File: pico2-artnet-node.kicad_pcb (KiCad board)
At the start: 2 copper layers, 84.6 x 157.4 mm, 59 parts, among them J2 NC3FAAH, J3 NC3FAAH, J4 NC3FAAH, J5 NC3FAAH, J6 USB_C_Receptacle_PowerOnly_6P, U1 W5500-EVB-PICO2, U2 CA-IS2092A, U3 CA-IS2092A, U4 CA-IS2092A, U5 CA-IS2092A, U6 WIZPoE Hat, U8 AMS1117-3.3

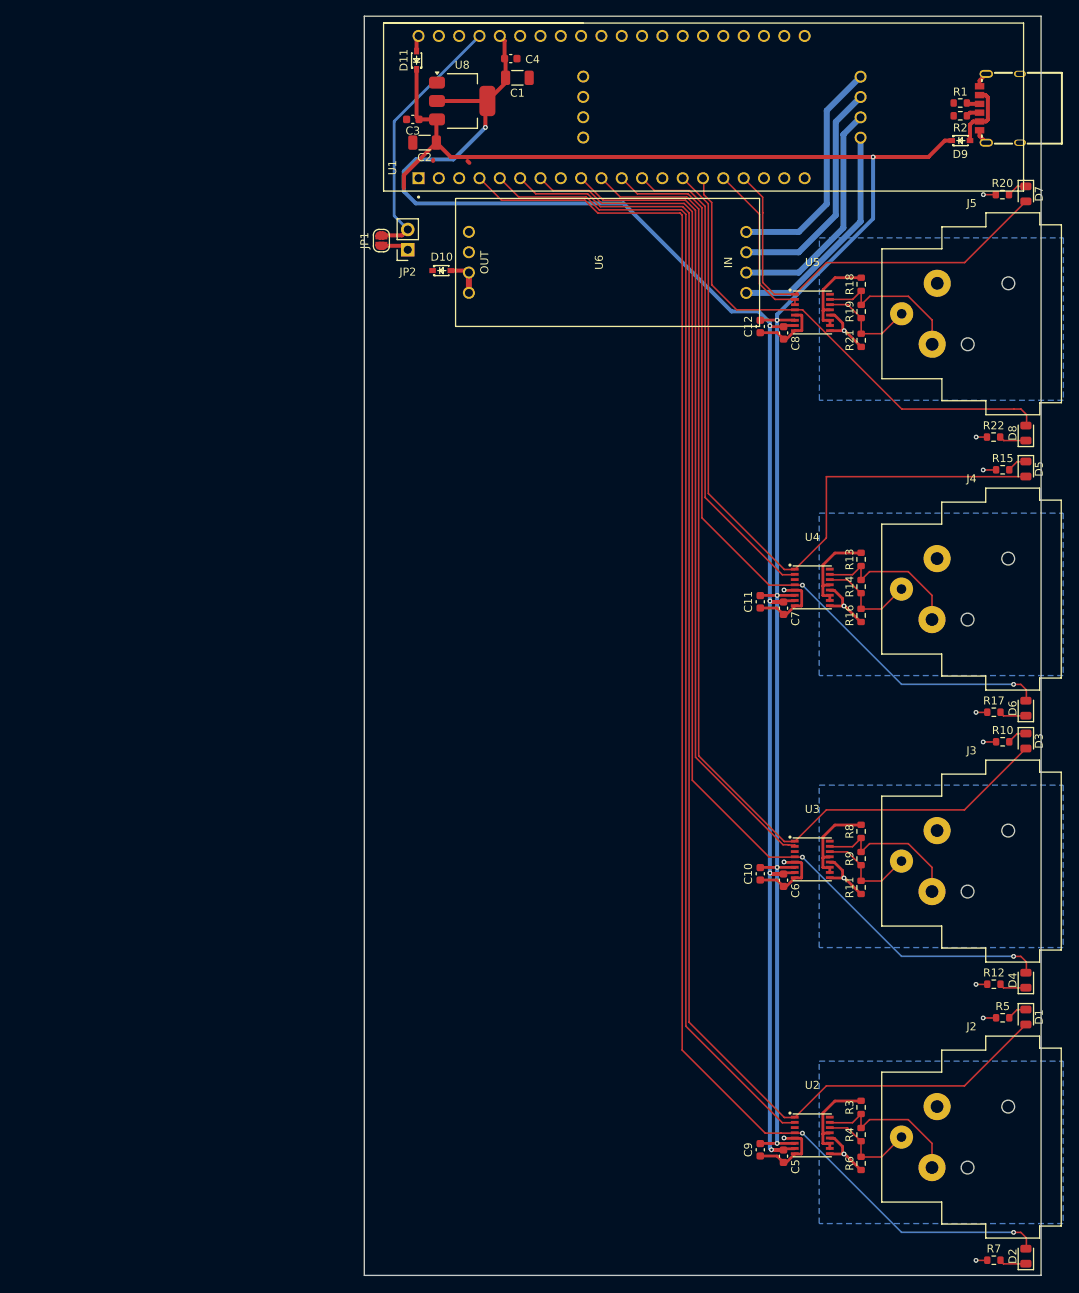
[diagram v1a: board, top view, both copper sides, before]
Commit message: v0.2 new DMX circuitry
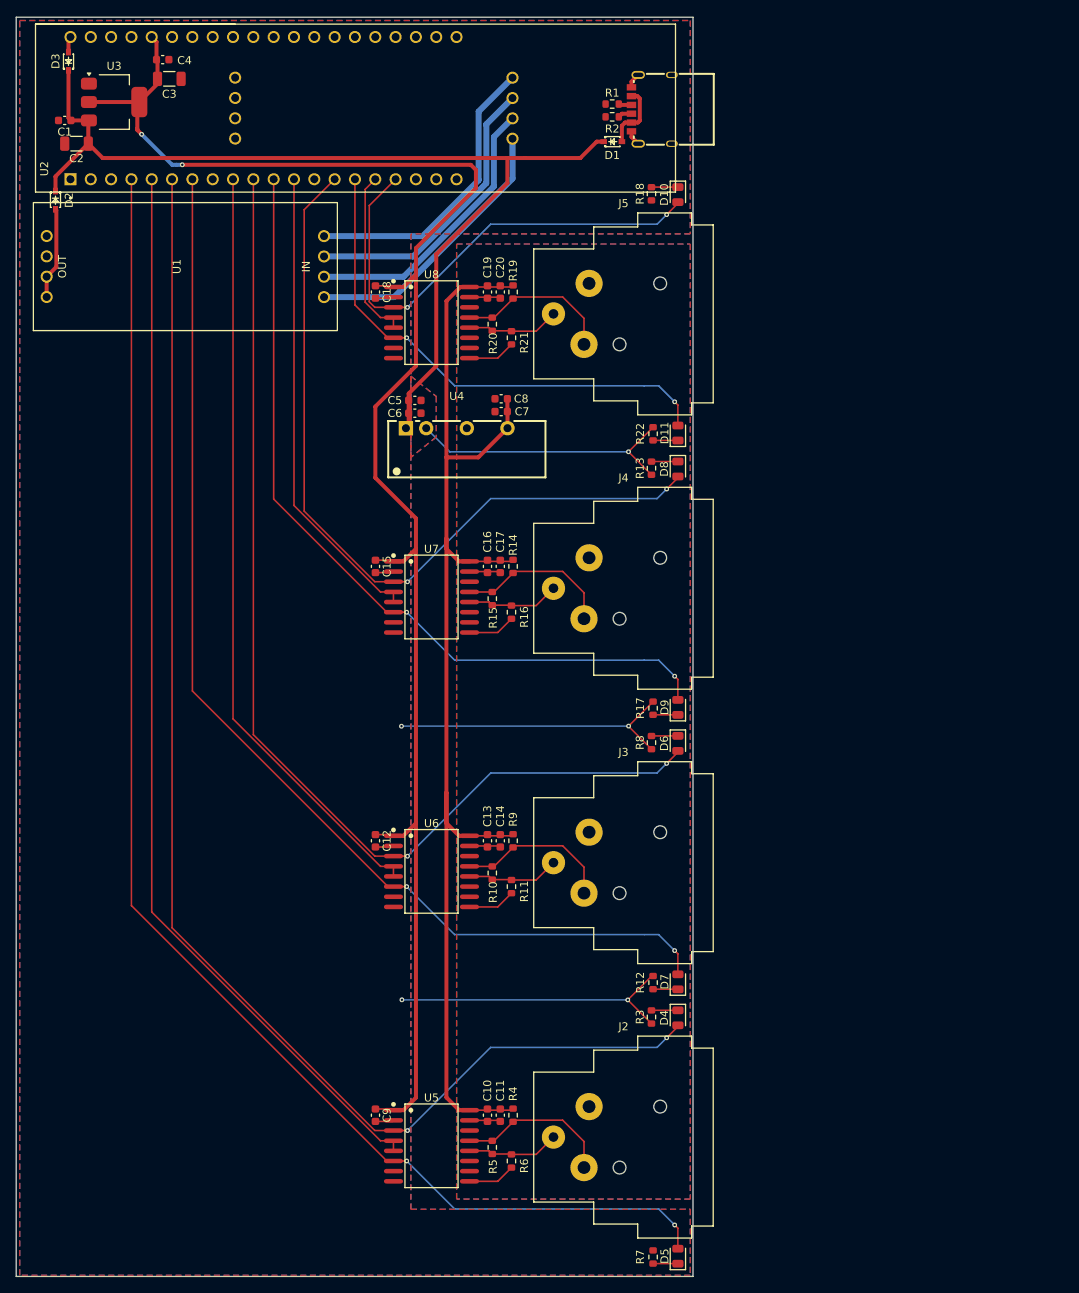
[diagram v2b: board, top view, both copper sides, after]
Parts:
- removed the D1 at (171.5, 159.8)
- removed the D2 at (171.5, 189.7)
- removed the D3 at (171.5, 125.3)
- removed JP1: disable onboard LDO, Jumper:SolderJumper-2_P1.3mm_Open_RoundedPad1.0x1.5mm
- removed JP2: disable onboard LDO, Connector_PinSocket_2.54mm:PinSocket_1x02_P2.54mm_Vertical
- removed the U2 at (144.8, 174.6)
- removed the U3 at (144.8, 140.1)
- added C13: 0.1u, Capacitor_SMD:C_0603_1608Metric, F.Cu at (104.2, 137.8)
- added C14: 10u, Capacitor_SMD:C_0603_1608Metric, F.Cu at (105.8, 137.8)
- added C15: 0.1u, Capacitor_SMD:C_0603_1608Metric, F.Cu at (90.2, 103.5)
- added C16: 0.1u, Capacitor_SMD:C_0603_1608Metric, F.Cu at (104.2, 103.5)
- added C17: 10u, Capacitor_SMD:C_0603_1608Metric, F.Cu at (105.8, 103.5)
- added C18: 0.1u, Capacitor_SMD:C_0603_1608Metric, F.Cu at (90.2, 69.2)
- added C19: 0.1u, Capacitor_SMD:C_0603_1608Metric, F.Cu at (104.2, 69.2)
- added C20: 10u, Capacitor_SMD:C_0603_1608Metric, F.Cu at (105.8, 69.2)
- added D10: YELLOW, LED_SMD:LED_0805_2012Metric, F.Cu at (128.0, 57.0)
- added D11: RED, LED_SMD:LED_0805_2012Metric, F.Cu at (128.0, 86.8)
- added D9: RED, LED_SMD:LED_0805_2012Metric, F.Cu at (128.0, 121.1)
- added U6: ISO1410BDWR, EasyEDA:SOIC-16_L10.3-W7.5-P1.27-LS10.3-BL, F.Cu at (97.2, 141.6)
- added U7: ISO1410BDWR, EasyEDA:SOIC-16_L10.3-W7.5-P1.27-LS10.3-BL, F.Cu at (97.2, 107.3)
- added U8: ISO1410BDWR, EasyEDA:SOIC-16_L10.3-W7.5-P1.27-LS10.3-BL, F.Cu at (97.2, 73.0)
- C10, C12, C6, C7, C9: value 10u -> 0.1u
- D4, D6, D8: value RED -> YELLOW
- D5, D7: value YELLOW -> RED
- R10, R15, R20, R5: value 75R -> 120R
- R12, R17, R22, R7: value 51R -> 56
- R13, R18, R3, R8: value 510R -> 56
- R14, R19, R4, R9: value 120R -> 510R
- U4: value CA-IS2092A -> B0505S-2WR3; footprint EasyEDA:LGA-16_L5.2-W4.7-P0.65-TL_CA-IS2062A-FRANK2 -> EasyEDA:PWRM-TH_BXXXXS-2WR3
- U5: value CA-IS2092A -> ISO1410BDWR; footprint EasyEDA:LGA-16_L5.2-W4.7-P0.65-TL_CA-IS2062A-FRANK2 -> EasyEDA:SOIC-16_L10.3-W7.5-P1.27-LS10.3-BL
- moved U5 114.5 mm to (97.2, 175.9), turned to -90 degrees
- moved D7 107.7 mm to (128.0, 155.4), turned to 90 degrees
- moved D5 107.6 mm to (128.0, 189.7), turned to 90 degrees
- moved C5 105.1 mm to (95.1, 82.7), turned to 180 degrees
- moved C12 80.3 mm to (90.2, 137.8)
- moved C6 74.4 mm to (95.1, 84.3), turned to 180 degrees
- moved C11 71.9 mm to (105.8, 172.1)
- moved R10 65.9 mm to (104.8, 141.8), turned to 90 degrees
- moved R5 65.8 mm to (104.8, 176.1), turned to 90 degrees
- moved R15 65.8 mm to (104.8, 107.5), turned to 90 degrees
- moved R20 65.8 mm to (104.8, 73.2), turned to 90 degrees
- moved U1 52.8 mm to (49.1, 69.8)
- moved D2 49.1 mm to (50.2, 57.7), turned to -90 degrees
- moved U4 48.7 mm to (100.3, 86.2)
- moved C9 48.3 mm to (90.2, 172.1)
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- renumbered C3 to C1, C1 to C3, D9 to D1, D10 to D2, D11 to D3, J6 to J1, U6 to U1, U1 to U2, U8 to U3
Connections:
- C10 pad 1: +5V -> +5VA
- C10 pad 2: GND -> GNDA
- C11 pad 1: +5V -> +5VA
- C11 pad 2: GND -> GNDA
- C12 pad 1: +5V -> +3V3
- C5 pad 1: +3V3 -> GND
- C5 pad 2: GND -> +5V
- C6 pad 1: +3V3 -> GND
- C6 pad 2: GND -> +5V
- C7 pad 1: +3V3 -> +5VA
- C7 pad 2: GND -> GNDA
- C8 pad 1: +3V3 -> +5VA
- C8 pad 2: GND -> GNDA
- C9 pad 1: +5V -> +3V3
- D4 pad 2: DMX2_TX -> DMX1_RX
- D5 pad 2: DMX3_RX -> DMX1_TX
- D6 pad 2: DMX3_TX -> DMX2_RX
- D7 pad 2: DMX4_RX -> DMX2_TX
- D8 pad 2: DMX4_TX -> DMX3_RX
- J2 pad 1: AGND -> GNDA
- J2 pad 2: Net-(U2-B) -> Net-(U5-B)
- J2 pad 3: Net-(U2-A) -> Net-(U5-A)
- J3 pad 1: AGND -> GNDA
- J3 pad 2: Net-(U3-B) -> Net-(U6-B)
- J3 pad 3: Net-(U3-A) -> Net-(U6-A)
- J4 pad 1: AGND -> GNDA
- J4 pad 2: Net-(U4-B) -> Net-(U7-B)
- J4 pad 3: Net-(U4-A) -> Net-(U7-A)
- J5 pad 1: AGND -> GNDA
- J5 pad 2: Net-(U5-B) -> Net-(U8-B)
- J5 pad 3: Net-(U5-A) -> Net-(U8-A)
- R10 pad 1: GND -> Net-(U6-A)
- R10 pad 2: Net-(D3-K) -> Net-(U6-B)
- R11 pad 1: AGND -> GNDA
- R11 pad 2: Net-(U3-A) -> Net-(U6-A)
- R12 pad 2: Net-(D4-K) -> Net-(D7-K)
- R13 pad 1: Net-(U4-B) -> GND
- R13 pad 2: +5VA -> Net-(D8-K)
- R14 pad 1: Net-(U4-A) -> Net-(U7-B)
- R14 pad 2: Net-(U4-B) -> +5VA
- R15 pad 1: GND -> Net-(U7-A)
- R15 pad 2: Net-(D5-K) -> Net-(U7-B)
- R16 pad 1: AGND -> GNDA
- R16 pad 2: Net-(U4-A) -> Net-(U7-A)
- R17 pad 2: Net-(D6-K) -> Net-(D9-K)
- R18 pad 1: Net-(U5-B) -> GND
- R18 pad 2: +5VA -> Net-(D10-K)
- R19 pad 1: Net-(U5-A) -> Net-(U8-B)
- R19 pad 2: Net-(U5-B) -> +5VA
- R20 pad 1: GND -> Net-(U8-A)
- R20 pad 2: Net-(D7-K) -> Net-(U8-B)
- R21 pad 1: AGND -> GNDA
- R21 pad 2: Net-(U5-A) -> Net-(U8-A)
- R22 pad 2: Net-(D8-K) -> Net-(D11-K)
- R3 pad 1: Net-(U2-B) -> GND
- R3 pad 2: +5VA -> Net-(D4-K)
- R4 pad 1: Net-(U2-A) -> Net-(U5-B)
- R4 pad 2: Net-(U2-B) -> +5VA
- R5 pad 1: GND -> Net-(U5-A)
- R5 pad 2: Net-(D1-K) -> Net-(U5-B)
- R6 pad 1: AGND -> GNDA
- R6 pad 2: Net-(U2-A) -> Net-(U5-A)
- R7 pad 2: Net-(D2-K) -> Net-(D5-K)
- R8 pad 1: Net-(U3-B) -> GND
- R8 pad 2: +5VA -> Net-(D6-K)
- R9 pad 1: Net-(U3-A) -> Net-(U6-B)
- R9 pad 2: Net-(U3-B) -> +5VA
- U2 pad 37: Net-(JP1-B) -> GND
- U4 pad 1: DMX3_RX -> +5V
- U4 pad 2: DMX3_DIR -> GND
- U4 pad 4: DMX3_TX -> GNDA
- U4 pad 6: +5V -> +5VA
- U5 pad 1: DMX4_RX -> +3V3
- U5 pad 10: +5VA -> unconnected-(U5-NC-Pad10)
- U5 pad 11: +5VA -> unconnected-(U5-NC-Pad11)
- U5 pad 12: AGND -> Net-(U5-A)
- U5 pad 13: +5VA -> Net-(U5-B)
- U5 pad 14: Net-(U5-A) -> unconnected-(U5-NC-Pad14)
- U5 pad 15: Net-(U5-B) -> GNDA
- U5 pad 16: unconnected-(U5-NC-Pad16) -> +5VA
- U5 pad 2: DMX4_DIR -> GND
- U5 pad 3: DMX4_DIR -> DMX1_RX
- U5 pad 4: DMX4_TX -> DMX1_DIR
- U5 pad 5: GND -> DMX1_DIR
- U5 pad 6: +5V -> DMX1_TX
- U5 pad 7: +3V3 -> unconnected-(U5-NC-Pad7)
- U5 pad 9: AGND -> GNDA
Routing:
- net +5VA: track 46.5 -> 153.8 mm
- net +5V: track 231.3 -> 124.2 mm, vias 5 -> 0
- net GND: track 57.9 -> 121.6 mm, vias 11 -> 5
- net GNDA: track 0.00 -> 39.5 mm
- net Net-(JP1-B): track 32.9 -> 0.00 mm
- net AGND: track 30.8 -> 0.00 mm, vias 4 -> 0
- net Net-(U8-B): track 0.00 -> 19.7 mm
- net Net-(U7-B): track 0.00 -> 19.7 mm
- net Net-(U6-B): track 0.00 -> 19.7 mm
- net Net-(U4-B): track 19.7 -> 0.00 mm
- net Net-(U2-B): track 19.7 -> 0.00 mm
- net Net-(U3-B): track 19.7 -> 0.00 mm
- net Net-(U3-A): track 12.6 -> 0.00 mm
- net Net-(U2-A): track 12.6 -> 0.00 mm
- net Net-(U4-A): track 12.6 -> 0.00 mm
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- added copper zone on B.Cu, net GND
- added copper zone on F.Cu, net GND
- added copper zone on B.Cu, net GNDA
- added copper zone on F.Cu, net GNDA
- removed copper zone on B.Cu, net AGND

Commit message: add levelshifter and silkscreen
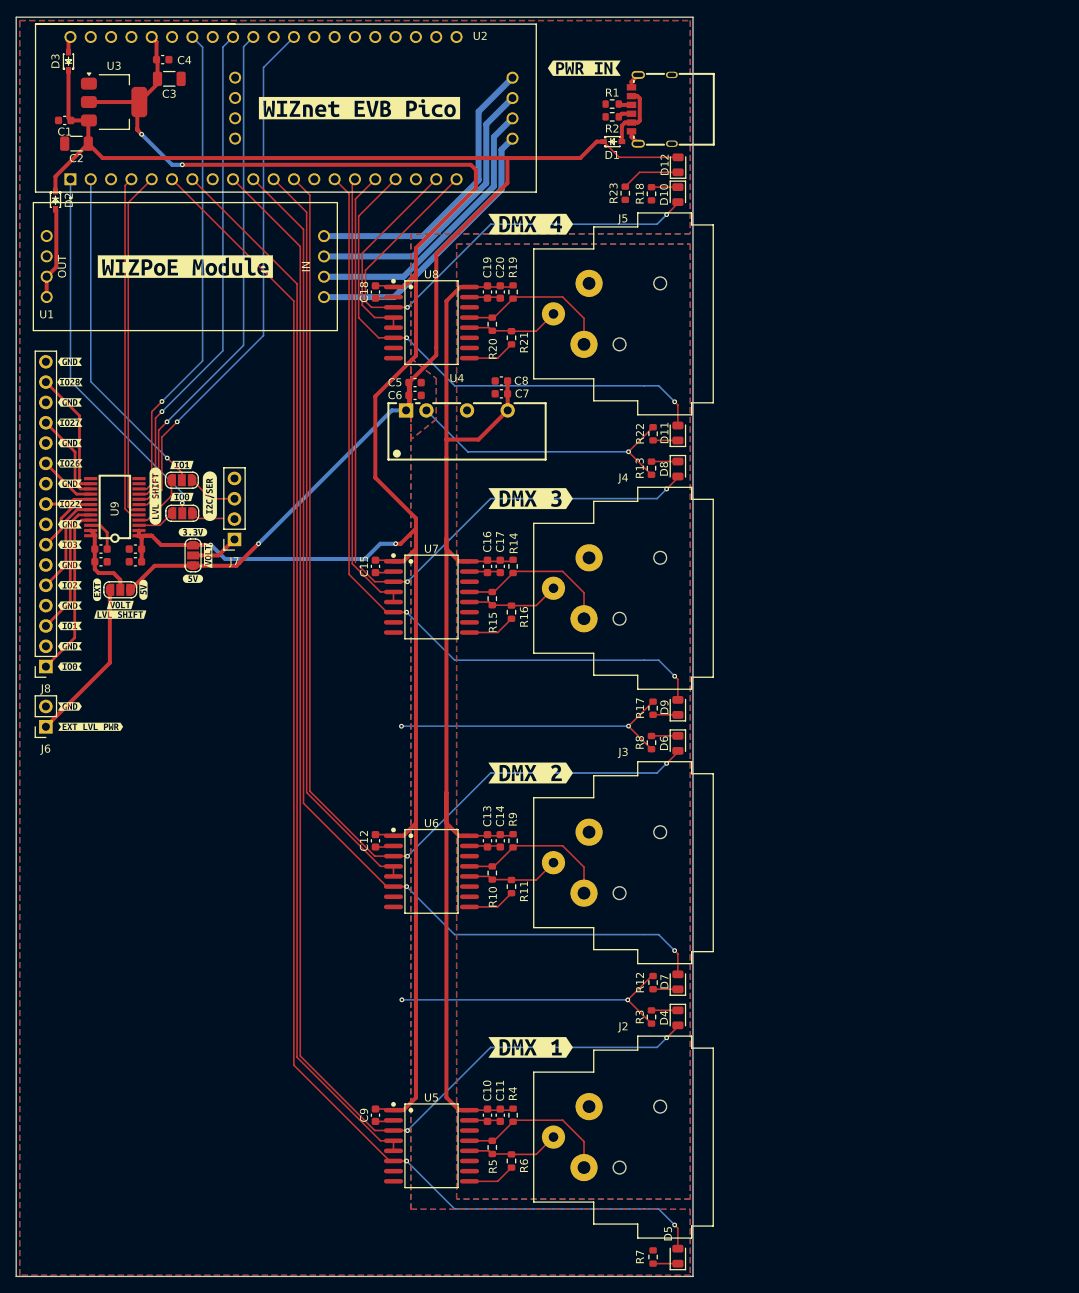
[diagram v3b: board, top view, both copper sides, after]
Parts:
- added C21: 10u, Capacitor_SMD:C_0603_1608Metric, F.Cu at (60.2, 102.9)
- added C22: 0.1u, Capacitor_SMD:C_0603_1608Metric, F.Cu at (60.2, 101.3)
- added C23: 10u, Capacitor_SMD:C_0603_1608Metric, F.Cu at (55.9, 101.3)
- added C24: 0.1u, Capacitor_SMD:C_0603_1608Metric, F.Cu at (55.9, 102.9)
- added D12: LED, LED_SMD:LED_0805_2012Metric, F.Cu at (128.0, 53.3)
- added J6: Conn_01x02_Pin, Connector_PinSocket_2.54mm:PinSocket_1x02_P2.54mm_Vertical, F.Cu at (49.0, 123.5)
- added J7: I2C Header, Connector_PinSocket_2.54mm:PinSocket_1x04_P2.54mm_Vertical, F.Cu at (72.6, 100.1)
- added J8: Conn_01x16_Pin, Connector_PinSocket_2.54mm:PinSocket_1x16_P2.54mm_Vertical, F.Cu at (49.0, 116.0)
- added JP1: SolderJumper_3_Open, Jumper:SolderJumper-3_P1.3mm_Open_RoundedPad1.0x1.5mm, F.Cu at (58.3, 106.4)
- added JP2: SolderJumper_3_Open, Jumper:SolderJumper-3_P1.3mm_Open_RoundedPad1.0x1.5mm, F.Cu at (66.0, 96.8)
- added JP3: SolderJumper_3_Open, Jumper:SolderJumper-3_P1.3mm_Open_RoundedPad1.0x1.5mm, F.Cu at (66.0, 92.7)
- added JP4: I2C Volt Sel, Jumper:SolderJumper-3_P1.3mm_Open_RoundedPad1.0x1.5mm, F.Cu at (67.4, 102.1)
- added R23: 82, Resistor_SMD:R_0603_1608Metric, F.Cu at (121.4, 56.8)
- added U9: SN74LVC4245APWR, EasyEDA:TSSOP-24_L7.8-W4.4-P0.65-LS6.4-BL, F.Cu at (57.6, 96.1)
- added kibuzzard-68DD1E8E: G***, kibuzzard-68DD1E8E, F.Cu at (66.0, 94.8)
- added kibuzzard-68DD1E9C: G***, kibuzzard-68DD1E9C, F.Cu at (66.0, 90.8)
- added kibuzzard-68DD1EE6: G***, kibuzzard-68DD1EE6, F.Cu at (69.3, 102.1)
- added kibuzzard-68DD1EFE: G***, kibuzzard-68DD1EFE, F.Cu at (62.7, 94.7)
- added kibuzzard-68DD1F08: G***, kibuzzard-68DD1F08, F.Cu at (69.5, 94.7)
- added kibuzzard-68DD1F80: G***, kibuzzard-68DD1F80, F.Cu at (67.4, 105.0)
- added kibuzzard-68DD1F80: G***, kibuzzard-68DD1F80, F.Cu at (61.2, 106.4)
- added kibuzzard-68DD1F8F: G***, kibuzzard-68DD1F8F, F.Cu at (67.4, 99.2)
- added kibuzzard-68DD21E1: G***, kibuzzard-68DD21E1, F.Cu at (52.0, 98.2)
- added kibuzzard-68DD21E1: G***, kibuzzard-68DD21E1, F.Cu at (52.0, 88.1)
- added kibuzzard-68DD21E1: G***, kibuzzard-68DD21E1, F.Cu at (52.0, 103.3)
- added kibuzzard-68DD21E1: G***, kibuzzard-68DD21E1, F.Cu at (52.0, 77.9)
- added kibuzzard-68DD21E1: G***, kibuzzard-68DD21E1, F.Cu at (52.0, 83.0)
- added kibuzzard-68DD21E1: G***, kibuzzard-68DD21E1, F.Cu at (52.0, 108.4)
- added kibuzzard-68DD21E1: G***, kibuzzard-68DD21E1, F.Cu at (52.0, 113.5)
- added kibuzzard-68DD21E1: G***, kibuzzard-68DD21E1, F.Cu at (52.0, 93.1)
- added kibuzzard-68DD227C: G***, kibuzzard-68DD227C, F.Cu at (52.0, 80.4)
- added kibuzzard-68DD228E: G***, kibuzzard-68DD228E, F.Cu at (52.0, 85.5)
- added kibuzzard-68DD2296: G***, kibuzzard-68DD2296, F.Cu at (52.0, 90.6)
- added kibuzzard-68DD22C2: G***, kibuzzard-68DD22C2, F.Cu at (52.0, 95.7)
- added kibuzzard-68DD22D5: G***, kibuzzard-68DD22D5, F.Cu at (52.0, 100.8)
- added kibuzzard-68DD22E0: G***, kibuzzard-68DD22E0, F.Cu at (52.0, 105.8)
- added kibuzzard-68DD22E9: G***, kibuzzard-68DD22E9, F.Cu at (52.0, 110.9)
- added kibuzzard-68DD22F0: G***, kibuzzard-68DD22F0, F.Cu at (52.0, 116.0)
- added kibuzzard-68DD2361: G***, kibuzzard-68DD2361, F.Cu at (55.4, 106.4)
- added kibuzzard-68DD23A7: G***, kibuzzard-68DD23A7, F.Cu at (58.3, 108.3)
- added kibuzzard-68DD23B6: G***, kibuzzard-68DD23B6, F.Cu at (58.3, 109.5)
- added kibuzzard-68DD2414: G***, kibuzzard-68DD2414, F.Cu at (109.6, 163.6)
- added kibuzzard-68DD244B: G***, kibuzzard-68DD244B, F.Cu at (109.6, 60.7)
- added kibuzzard-68DD245B: G***, kibuzzard-68DD245B, F.Cu at (109.6, 129.3)
- added kibuzzard-68DD2461: G***, kibuzzard-68DD2461, F.Cu at (109.6, 95.0)
- added kibuzzard-68DD286D: G***, kibuzzard-68DD286D, F.Cu at (66.4, 66.0)
- added kibuzzard-68DD28CA: G***, kibuzzard-68DD28CA, F.Cu at (88.2, 46.2)
- added kibuzzard-68DD2906: G***, kibuzzard-68DD2906, F.Cu at (52.0, 121.0)
- added kibuzzard-68DD2926: G***, kibuzzard-68DD2926, F.Cu at (54.6, 123.5)
- added kibuzzard-68DD3F78: G***, kibuzzard-68DD3F78, F.Cu at (116.3, 41.2)
- moved C6 2.23 mm to (95.1, 82.1)
- moved C8 2.23 mm to (105.9, 80.3)
- moved U4 2.23 mm to (100.4, 84.0)
- moved C5 2.23 mm to (95.1, 80.5)
- moved C7 2.23 mm to (105.9, 81.9)
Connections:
- U2 pad 1: unconnected-(U2-GP0-Pad1) -> GPIO0
- U2 pad 10: DMX2_RX -> DMX2_TX
- U2 pad 11: DMX3_TX -> DMX2_DIR
- U2 pad 12: DMX3_DIR -> DMX2_RX
- U2 pad 14: DMX3_RX -> DMX3_TX
- U2 pad 15: DMX4_TX -> DMX3_DIR
- U2 pad 16: DMX4_DIR -> DMX3_RX
- U2 pad 17: DMX4_RX -> DMX4_TX
- U2 pad 19: unconnected-(U2-GP14-Pad19) -> DMX4_DIR
- U2 pad 2: unconnected-(U2-GP1-Pad2) -> GPIO1
- U2 pad 20: unconnected-(U2-GP15-Pad20) -> DMX4_RX
- U2 pad 29: unconnected-(U2-GP22-Pad29) -> GPIO22
- U2 pad 31: unconnected-(U2-GP26-Pad31) -> GPIO26
- U2 pad 32: unconnected-(U2-GP27-Pad32) -> GPIO27
- U2 pad 34: unconnected-(U2-GP28-Pad34) -> GPIO28
- U2 pad 4: DMX1_TX -> GPIO2
- U2 pad 5: DMX1_DIR -> GPIO3
- U2 pad 6: DMX1_RX -> DMX1_TX
- U2 pad 7: DMX2_TX -> DMX1_DIR
- U2 pad 9: DMX2_DIR -> DMX1_RX
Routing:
- net GPIO22: track 0.00 -> 67.1 mm, vias 0 -> 1
- net GPIO26: track 0.00 -> 64.3 mm, vias 0 -> 1
- net GPIO27: track 0.00 -> 62.6 mm, vias 0 -> 1
- net GPIO28: track 0.00 -> 60.9 mm, vias 0 -> 1
- net +5V: track 124.2 -> 175.9 mm, vias 0 -> 1
- net GPIO0: track 0.00 -> 47.5 mm, vias 0 -> 1
- net GPIO3: track 0.00 -> 43.7 mm
- net GPIO2: track 0.00 -> 43.6 mm
- net +3V3: track 210.0 -> 252.7 mm, vias 2 -> 4
- net GPIO1: track 0.00 -> 42.6 mm, vias 0 -> 1
- net LVL SHIFT B1: track 0.00 -> 21.3 mm
- net Net-(J6-Pin_1): track 0.00 -> 20.4 mm
- net LVL SHIFT B2: track 0.00 -> 17.1 mm
- net LVL SHIFT B8: track 0.00 -> 15.7 mm
- net LVL SHIFT B3: track 0.00 -> 12.8 mm
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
